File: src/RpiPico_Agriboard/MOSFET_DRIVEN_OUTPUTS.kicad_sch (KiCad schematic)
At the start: 7 parts, among them J12 Conn_02x03_Odd_Even, J23 Screw_Terminal_01x02, Q5 AP3404

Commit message: schematic updates completed
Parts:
- R44: value 1K -> 100R
- R45: value 10K -> 100K
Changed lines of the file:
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@@
   (symbol (lib_id "Device:R_US") (at 106.68 87.63 90) (unit 1)
     (in_bom yes) (on_board yes) (dnp no) (fields_autoplaced)
-    (property "Reference" "R44" (at 106.68 81.28 90)
+    (property "Reference" "R44" (at 106.68 82.55 90)
       (effects (font (size 1.27 1.27)))
     )
-    (property "Value" "1K" (at 106.68 83.82 90)
+    (property "Value" "100R" (at 106.68 85.09 90)
       (effects (font (size 1.27 1.27)))
     )
@@
   (symbol (lib_id "Device:R_US") (at 112.395 95.25 0) (unit 1)
     (in_bom yes) (on_board yes) (dnp no) (fields_autoplaced)
-    (property "Reference" "R45" (at 114.3 93.9799 0)
+    (property "Reference" "R45" (at 114.3 94.615 0)
       (effects (font (size 1.27 1.27)) (justify left))
     )
-    (property "Value" "10K" (at 114.3 96.5199 0)
+    (property "Value" "100K" (at 114.3 97.155 0)
       (effects (font (size 1.27 1.27)) (justify left))
     )

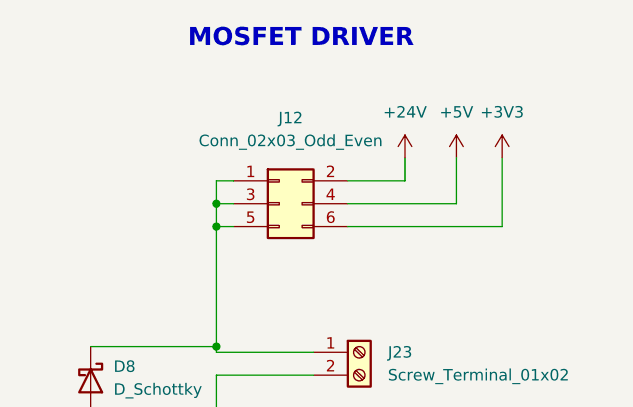
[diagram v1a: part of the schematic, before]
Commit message: layut updates, 3v3 sensor pwr updates
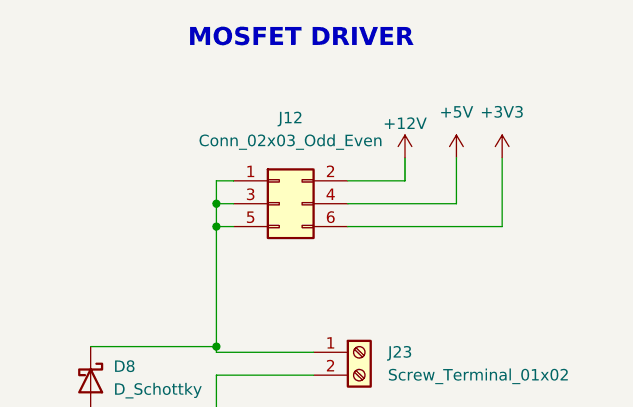
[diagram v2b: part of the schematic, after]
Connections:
- net +24V renamed +12V
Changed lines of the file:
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@@
     )
   )
-  (symbol (lib_id "power:+24V") (at 150.495 40.005 0) (mirror y) (unit 1)
+  (symbol (lib_id "power:+12V") (at 150.495 40.005 0) (unit 1)
     (in_bom yes) (on_board yes) (dnp no) (fields_autoplaced)
-    (property "Reference" "#PWR0128" (at 150.495 43.815 0)
+    (property "Reference" "#PWR091" (at 150.495 43.815 0)
       (effects (font (size 1.27 1.27)) hide)
     )
-    (property "Value" "+24V" (at 150.495 34.925 0)
+    (property "Value" "+12V" (at 150.495 36.195 0)
       (effects (font (size 1.27 1.27)))
     )
@@
     (instances
       (project "RpiPico_Agriboard"
-        (path "/c2474b65-c0e8-4987-86b2-fddddd4113dc/409c313f-e246-4e4c-98bc-c54a0aafafc3"
-          (reference "#PWR0128") (unit 1)
+        (path "/c2474b65-c0e8-4987-86b2-fddddd4113dc"
+          (reference "#PWR091") (unit 1)
         )
         (path "/c2474b65-c0e8-4987-86b2-fddddd4113dc/d7235480-5339-47ed-bac5-b2c207ca2fef"
-          (reference "#PWR0110") (unit 1)
+          (reference "#PWR043") (unit 1)
+        )
+        (path "/c2474b65-c0e8-4987-86b2-fddddd4113dc/409c313f-e246-4e4c-98bc-c54a0aafafc3"
+          (reference "#PWR069") (unit 1)
         )
         (path "/c2474b65-c0e8-4987-86b2-fddddd4113dc/c2ae985f-4241-4ec2-979d-cb385c950bc9"
-          (reference "#PWR0130") (unit 1)
+          (reference "#PWR071") (unit 1)
         )
       )
